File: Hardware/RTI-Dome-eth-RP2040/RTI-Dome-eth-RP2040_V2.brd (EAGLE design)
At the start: 111.1 x 76.3 mm, 106 parts, among them IC1 REG1117FA-5.0_500, IC2 24LC64T-I/SN, IC3 FT232RL, IC4 RASPBERRY_PI_PICO, IC8 REG1117-3.3V, J2 XT60PW-M, T1 MMBT3904LT1, T2 MMBT3904LT1, T3 MMBT3904LT1, U1 W5500, X13 PN61729-S, X9 J1011F01PNL

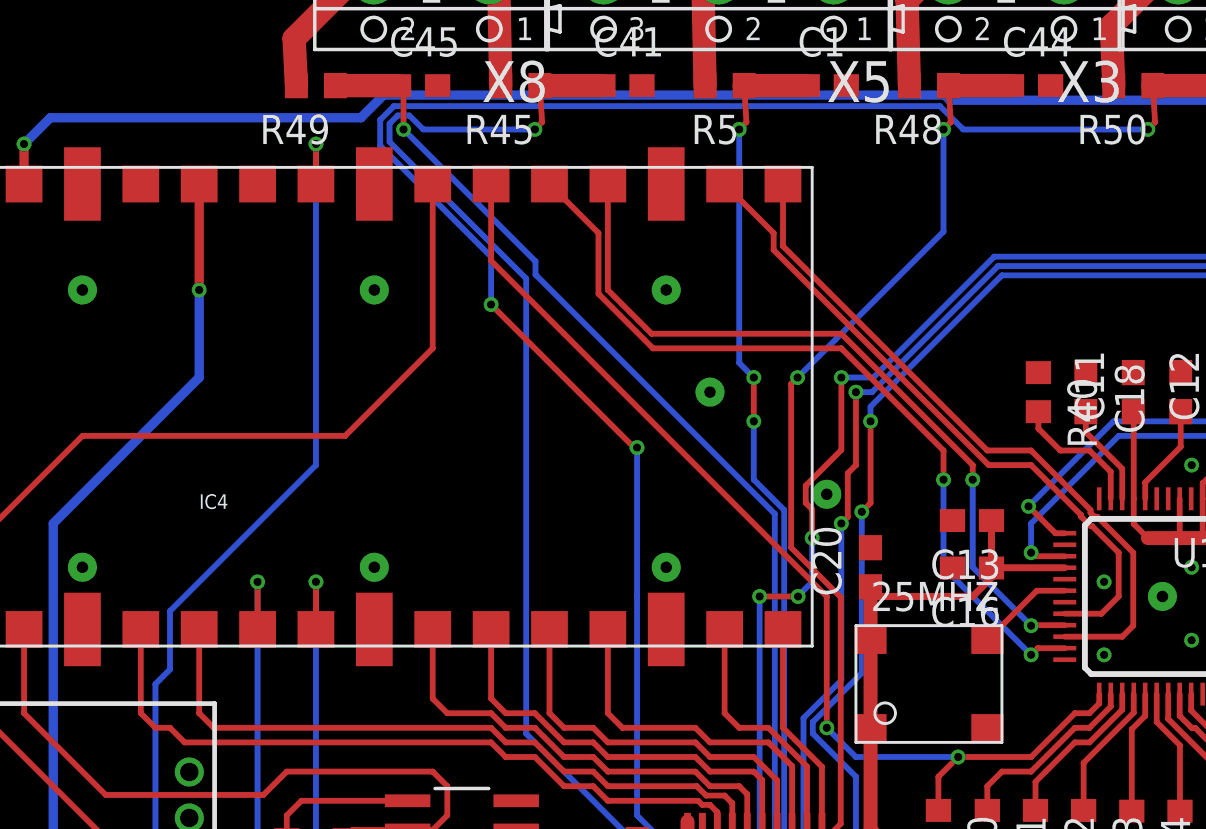
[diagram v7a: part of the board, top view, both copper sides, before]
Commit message: Adding the same code for the RP2040 but using the lwIP_w5500 lib.
This is still not 100% functional as the same code is 25 times
slower to respond to queries. Next step is to wire the INT pin
on the PCB to try to address this issue.
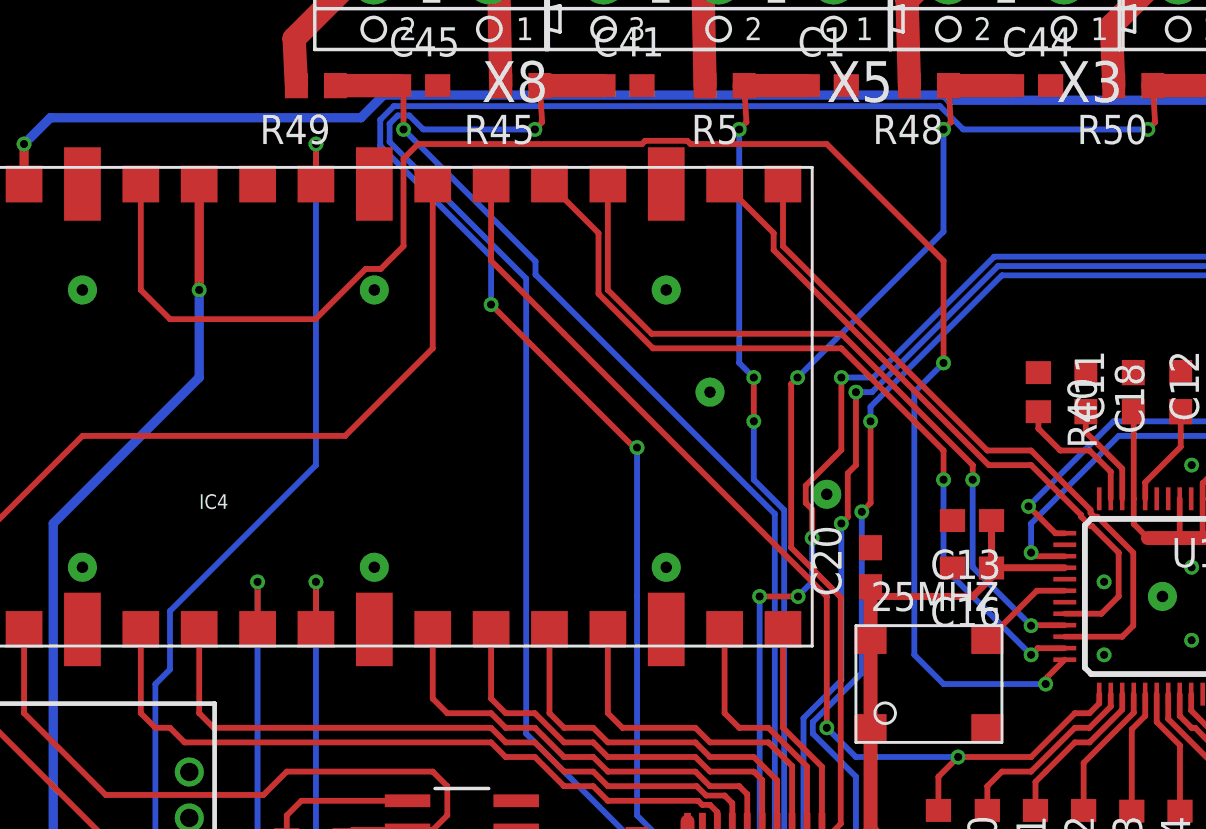
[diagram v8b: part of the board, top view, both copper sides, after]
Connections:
- net N$59 renamed ADC_REF
- net N$60 renamed 3V3_OUT
- net N$61 renamed 3V3_EN
- net N$64 renamed VBUS
- removed net N$56: IC4.32
- net INT_N: now also IC4.32
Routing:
- net INT_N: track 0.00 -> 73.0 mm, vias 0 -> 2
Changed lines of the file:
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@@
 <signal name="INT_N">
 <contactref element="U1" pad="36"/>
+<contactref element="IC4" pad="32"/>
+<wire x1="61.79" y1="39.795" x2="60.96" y2="38.965" width="0.254" layer="1"/>
+<wire x1="60.96" y1="38.965" x2="60.96" y2="38.735" width="0.254" layer="1"/>
+<via x="60.96" y="38.735" extent="1-16" drill="0.35"/>
+<via x="56.515" y="52.705" extent="1-16" drill="0.35"/>
+<wire x1="56.515" y1="57.15" x2="56.515" y2="52.705" width="0.254" layer="1"/>
+<wire x1="56.515" y1="57.15" x2="51.435" y2="62.23" width="0.254" layer="1"/>
+<wire x1="33.655" y1="62.23" x2="33.02" y2="61.595" width="0.254" layer="1"/>
+<wire x1="51.435" y1="62.23" x2="45.50513125" y2="62.23" width="0.254" layer="1"/>
+<wire x1="45.50513125" y1="62.23" x2="45.36573125" y2="62.3694" width="0.254" layer="1"/>
+<wire x1="45.36573125" y1="62.3694" x2="43.53426875" y2="62.3694" width="0.254" layer="1"/>
+<wire x1="43.53426875" y1="62.3694" x2="43.39486875" y2="62.23" width="0.254" layer="1"/>
+<wire x1="43.39486875" y1="62.23" x2="33.655" y2="62.23" width="0.254" layer="1"/>
+<wire x1="33.02" y1="61.595" x2="33.02" y2="57.785" width="0.254" layer="1"/>
+<wire x1="33.02" y1="57.785" x2="32.0294" y2="56.7944" width="0.254" layer="1"/>
+<wire x1="32.0294" y1="56.7944" x2="31.3712375" y2="56.7944" width="0.254" layer="1"/>
+<wire x1="29.1868375" y1="54.61" x2="22.86" y2="54.61" width="0.254" layer="1"/>
+<wire x1="31.3712375" y1="56.7944" x2="29.1868375" y2="54.61" width="0.254" layer="1"/>
+<wire x1="22.86" y1="54.61" x2="21.59" y2="55.88" width="0.254" layer="1"/>
+<wire x1="21.59" y1="55.88" x2="21.59" y2="60.49" width="0.254" layer="1"/>
+<wire x1="60.96" y1="38.735" x2="56.515" y2="38.735" width="0.254" layer="16"/>
+<wire x1="56.515" y1="38.735" x2="55.245" y2="40.005" width="0.254" layer="16"/>
+<wire x1="55.245" y1="40.005" x2="55.245" y2="51.435" width="0.254" layer="16"/>
+<wire x1="55.245" y1="51.435" x2="56.515" y2="52.705" width="0.254" layer="16"/>
 </signal>
 <signal name="N$17">
@@
 <wire x1="91.8464" y1="70.28" x2="91.8464" y2="64.8564" width="1.016" layer="1"/>
 </signal>
-<signal name="N$56">
-<contactref element="IC4" pad="32"/>
-</signal>
-<signal name="N$59">
+<signal name="ADC_REF">
 <contactref element="IC4" pad="35"/>
 </signal>
-<signal name="N$60">
+<signal name="3V3_OUT">
 <contactref element="IC4" pad="36"/>
 </signal>
-<signal name="N$61">
+<signal name="3V3_EN">
 <contactref element="IC4" pad="37"/>
 </signal>
-<signal name="N$64">
+<signal name="VBUS">
 <contactref element="IC4" pad="40"/>
 </signal>
